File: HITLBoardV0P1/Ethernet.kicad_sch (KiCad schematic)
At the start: 36 parts, among them U2 LAN8650B1-E/LMX, U3 LP38852MRX-ADJ/NOPB

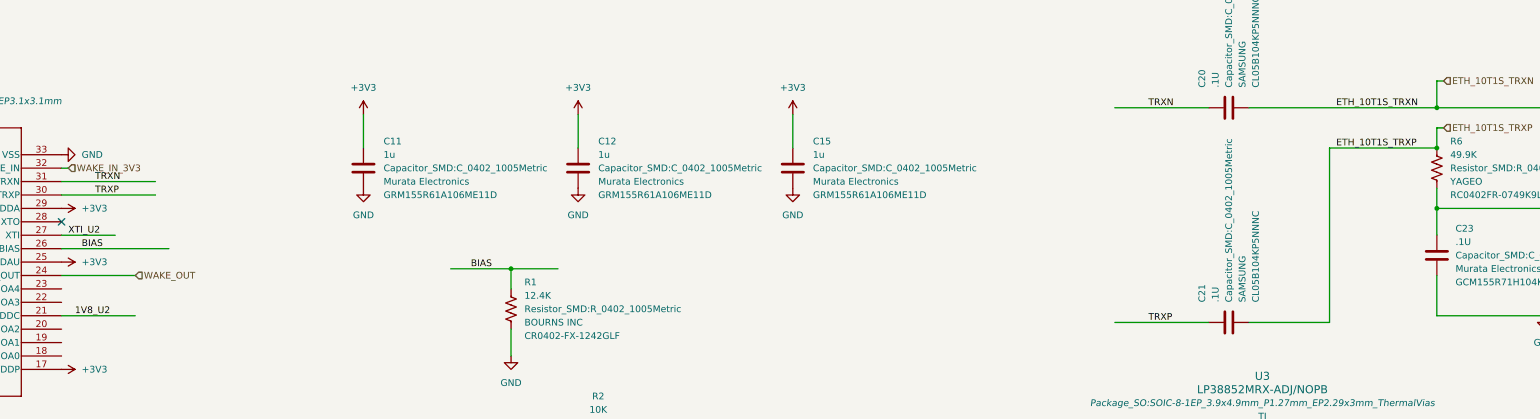
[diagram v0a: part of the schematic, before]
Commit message: MINOR UPDATES -- SWTICH ONE LAN TO SPI 5 INSTEAD OF SPI1 ON THE TMDX, SET UP LAN8650S for actual differential pair routing by changing suffix to "_DN" and "_DP" instead of "_N" or "_P" or just "N", "P"
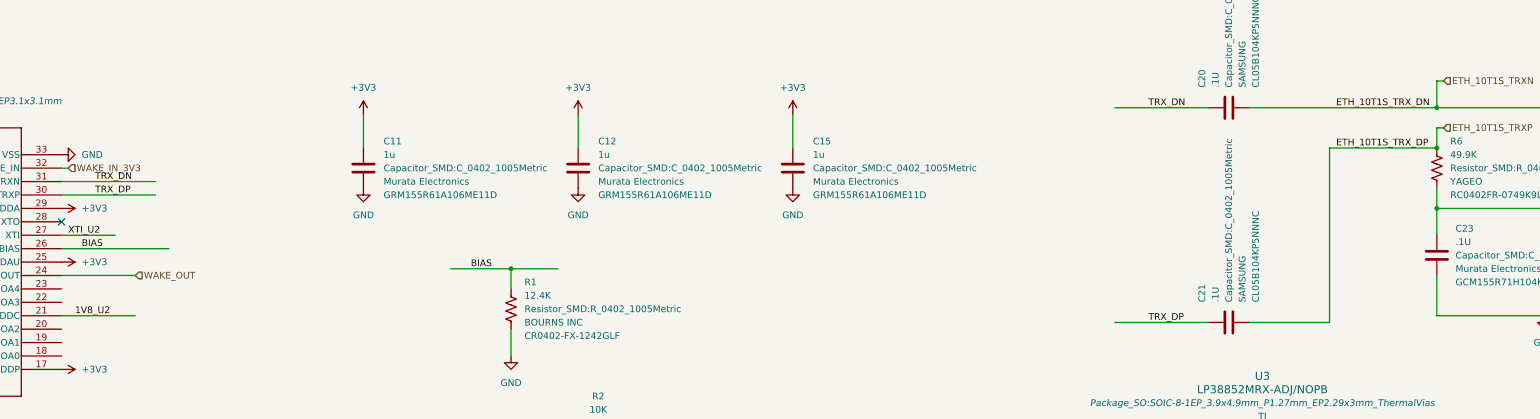
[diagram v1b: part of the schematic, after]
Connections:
- net TRXN renamed TRX_DN
- net TRXP renamed TRX_DP
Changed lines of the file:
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@@
 		)
 	)
-	(label "TRXP"
+	(label "TRX_DP"
 		(at 105.41 54.61 0)
 		(effects
@@
 		)
 	)
-	(label "ETH_10T1S_TRXN"
+	(label "ETH_10T1S_TRX_DN"
 		(at 340.36 38.1 0)
 		(effects
@@
 		)
 	)
-	(label "TRXN"
+	(label "TRX_DN"
 		(at 105.41 52.07 0)
 		(effects
@@
 		)
 	)
-	(label "TRXN"
+	(label "TRX_DN"
 		(at 304.8 38.1 0)
 		(effects
@@
 		)
 	)
-	(label "ETH_10T1S_TRXP"
+	(label "ETH_10T1S_TRX_DP"
 		(at 340.36 45.72 0)
 		(effects
@@
 		)
 	)
-	(label "TRXP"
+	(label "TRX_DP"
 		(at 304.8 78.74 0)
 		(effects

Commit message: fix ethernet channel that was fubar, beginning layout
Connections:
- net +3V3: no longer C10.1, C5.1, C6.1, C7.1, C8.1, C9.1
- net 1V8_U2: now also C10.1, C5.1, C6.1, C7.1, C8.1, C9.1
- no-connect marks 2 -> 3
